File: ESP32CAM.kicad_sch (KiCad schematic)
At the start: 16 parts, among them J12 USB_C_Receptacle_USB2.0, SW6 SW_Push, U11 FT231XS, U12 ESP32-CAM

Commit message: Nearly done schematics
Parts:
- renumbered C24 to C25, C25 to C26, C26 to C27, C27 to C28, C28 to C29, SW6 to SW5
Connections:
- net 3.3V_Out: no longer R29.2, R30.1, U11.11 (USBDP), U11.12 (USBDM)
- new net: R30.1, U11.11 (USBDP)
- new net: R29.2, U11.12 (USBDM)

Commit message: Much much more progress
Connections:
- net 3.3V_Out: now also R29.2, R30.1, U11.11 (USBDP), U11.12 (USBDM)
- net ESPCAM_MISO: now also U12.P$12 (GPIO13); no longer U12.P$11 (GPIO12)
- net ESPCAM_MOSI: now also U12.P$11 (GPIO12); no longer U12.P$12 (GPIO13)
- net Earth: no longer SW5.2
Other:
- note added: "MISO"
- note added: "MOSI"
- moved on the sheet: C29, SW5, U12

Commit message: Rev 1
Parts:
- removed C29: 0.1uF, Capacitor_SMD:C_0402_1005Metric, symbol Device:C_Small
- removed R31: 1M, Resistor_SMD:R_0402_1005Metric, symbol Device:R_US
- removed SW5: SW_Push, Button_Switch_SMD:SW_SPST_PTS645, symbol Switch:SW_Push
- added J10: Conn_01x02, Connector_PinHeader_2.54mm:PinHeader_1x02_P2.54mm_Vertical, symbol Connector_Generic:Conn_01x02
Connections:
- net 3.3V_Out: no longer R29.2, R30.1, U11.11 (USBDP), U11.12 (USBDM)
- net Earth: now also J12.S1 (SHIELD), J10.1 (Pin_1)
- net at U12.P$6 (GPIO0): now also J10.2 (Pin_2)
- new net: R30.1, U11.11 (USBDP)
- new net: R29.2, U11.12 (USBDM)
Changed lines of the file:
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@@
   (junction (at 149.606 75.184) (diameter 0) (color 0 0 0 0)
-  )
-  (junction (at 129.286 44.704) (diameter 0) (color 0 0 0 0)
-  )
-  (junction (at 167.259 130.302) (diameter 0) (color 0 0 0 0)
-  )
-  (junction (at 129.286 47.244) (diameter 0) (color 0 0 0 0)
   )
   (junction (at 129.286 37.084) (diameter 0) (color 0 0 0 0)
@@
     (stroke (width 0) (type default))
   )
-  (wire (pts (xy 129.286 44.704) (xy 129.286 47.244))
-    (stroke (width 0) (type default))
-  )
-  (wire (pts (xy 25.4 66.04) (xy 25.4 65.405))
-    (stroke (width 0) (type default))
-  )
   (wire (pts (xy 131.826 20.574) (xy 138.176 20.574))
     (stroke (width 0) (type default))
@@
     (stroke (width 0) (type default))
   )
-  (wire (pts (xy 129.286 37.084) (xy 129.286 44.704))
+  (wire (pts (xy 129.286 37.084) (xy 129.286 52.324))
     (stroke (width 0) (type default))
   )
@@
     (stroke (width 0) (type default))
   )
-  (wire (pts (xy 169.799 134.112) (xy 167.259 134.112))
-    (stroke (width 0) (type default))
-  )
   (wire (pts (xy 57.15 45.085) (xy 48.26 45.085))
     (stroke (width 0) (type default))
@@
     (stroke (width 0) (type default))
   )
-  (wire (pts (xy 167.259 130.302) (xy 167.259 134.112))
-    (stroke (width 0) (type default))
-  )
   (wire (pts (xy 105.029 130.302) (xy 112.014 130.302))
     (stroke (width 0) (type default))
@@
     (stroke (width 0) (type default))
   )
-  (wire (pts (xy 174.879 134.112) (xy 177.419 134.112))
-    (stroke (width 0) (type default))
-  )
   (wire (pts (xy 113.411 44.704) (xy 115.316 44.704))
     (stroke (width 0) (type default))
@@
     (stroke (width 0) (type default))
   )
-  (wire (pts (xy 129.286 47.244) (xy 129.286 52.324))
-    (stroke (width 0) (type default))
-  )
   (wire (pts (xy 48.26 40.005) (xy 48.26 42.545))
     (stroke (width 0) (type default))
@@
     (stroke (width 0) (type default))
   )
+  (wire (pts (xy 167.259 136.017) (xy 167.259 132.842))
+    (stroke (width 0) (type default))
+  )
   (wire (pts (xy 121.666 37.084) (xy 121.666 36.449))
     (stroke (width 0) (type default))
@@
     (stroke (width 0) (type default))
   )
-  (wire (pts (xy 25.4 73.66) (xy 25.4 74.93))
+  (wire (pts (xy 25.4 65.405) (xy 25.4 74.93))
     (stroke (width 0) (type default))
   )
@@
     )
   )
-  (symbol (lib_id "Switch:SW_Push") (at 172.339 130.302 0) (unit 1)
-    (in_bom yes) (on_board yes) (dnp no) (fields_autoplaced)
-    (property "Reference" "SW5" (at 172.339 122.047 0)
-      (effects (font (size 1.27 1.27)))
-    )
-    (property "Value" "SW_Push" (at 172.339 124.587 0)
-      (effects (font (size 1.27 1.27)))
-    )
-    (property "Footprint" "Button_Switch_SMD:SW_SPST_PTS645" (at 172.339 125.222 0)
-      (effects (font (size 1.27 1.27)) hide)
-    )
-    (property "Datasheet" "~" (at 172.339 125.222 0)
-      (effects (font (size 1.27 1.27)) hide)
-    )
-    (pin "1")
-    (pin "2")
-    (instances
-      (project "DeltaRhoRobot"
-        (path "/cced1a6d-3dc4-42b2-93bd-998a7b4cf4e8/5eb80655-957d-4a1c-8d7d-b2e173715026/ba807c80-2a51-4f5f-8aa4-02e2ddffef6a"
-          (reference "SW5") (unit 1)
-        )
-      )
-    )
-  )
-  (symbol (lib_id "power:Earth") (at 177.419 134.112 0) (unit 1)
-    (in_bom yes) (on_board yes) (dnp no) (fields_autoplaced)
-    (property "Reference" "#PWR0104" (at 177.419 140.462 0)
-      (effects (font (size 1.27 1.27)) hide)
-    )
-    (property "Value" "Earth" (at 177.419 137.922 0)
-      (effects (font (size 1.27 1.27)) hide)
-    )
-    (property "Footprint" "" (at 177.419 134.112 0)
-      (effects (font (size 1.27 1.27)) hide)
-    )
-    (property "Datasheet" "~" (at 177.419 134.112 0)
+  (symbol (lib_id "power:Earth") (at 167.259 136.017 0) (unit 1)
+    (in_bom yes) (on_board yes) (dnp no) (fields_autoplaced)
+    (property "Reference" "#PWR0104" (at 167.259 142.367 0)
+      (effects (font (size 1.27 1.27)) hide)
+    )
+    (property "Value" "Earth" (at 167.259 139.827 0)
+      (effects (font (size 1.27 1.27)) hide)
+    )
+    (property "Footprint" "" (at 167.259 136.017 0)
+      (effects (font (size 1.27 1.27)) hide)
+    )
+    (property "Datasheet" "~" (at 167.259 136.017 0)
       (effects (font (size 1.27 1.27)) hide)
     )
@@
     )
   )
-  (symbol (lib_id "Device:C_Small") (at 172.339 134.112 270) (unit 1)
-    (in_bom yes) (on_board yes) (dnp no)
-    (property "Reference" "C29" (at 169.164 137.287 90)
-      (effects (font (size 1.27 1.27)) (justify left))
-    )
-    (property "Value" "0.1uF" (at 169.164 139.192 90)
-      (effects (font (size 1.27 1.27)) (justify left))
-    )
-    (property "Footprint" "Capacitor_SMD:C_0402_1005Metric" (at 172.339 134.112 0)
-      (effects (font (size 1.27 1.27)) hide)
-    )
-    (property "Datasheet" "~" (at 172.339 134.112 0)
-      (effects (font (size 1.27 1.27)) hide)
-    )
-    (pin "1")
-    (pin "2")
-    (instances
-      (project "DeltaRhoRobot"
-        (path "/cced1a6d-3dc4-42b2-93bd-998a7b4cf4e8/5eb80655-957d-4a1c-8d7d-b2e173715026/ba807c80-2a51-4f5f-8aa4-02e2ddffef6a"
-          (reference "C29") (unit 1)
-        )
-      )
-    )
-  )
   (symbol (lib_id "power:Earth") (at 164.719 123.317 0) (mirror y) (unit 1)
     (in_bom yes) (on_board yes) (dnp no) (fields_autoplaced)
@@
         (path "/cced1a6d-3dc4-42b2-93bd-998a7b4cf4e8/5eb80655-957d-4a1c-8d7d-b2e173715026/ba807c80-2a51-4f5f-8aa4-02e2ddffef6a"
           (reference "R29") (unit 1)
+        )
+      )
+    )
+  )
+  (symbol (lib_id "Connector_Generic:Conn_01x02") (at 172.339 132.842 0) (mirror x) (unit 1)
+    (in_bom yes) (on_board yes) (dnp no)
+    (property "Reference" "J10" (at 175.26 132.842 0)
+      (effects (font (size 1.27 1.27)) (justify left))
+    )
+    (property "Value" "Conn_01x02" (at 175.26 130.302 0)
+      (effects (font (size 1.27 1.27)) (justify left))
+    )
+    (property "Footprint" "Connector_PinHeader_2.54mm:PinHeader_1x02_P2.54mm_Vertical" (at 172.339 132.842 0)
+      (effects (font (size 1.27 1.27)) hide)
+    )
+    (property "Datasheet" "~" (at 172.339 132.842 0)
+      (effects (font (size 1.27 1.27)) hide)
+    )
+    (pin "1")
+    (pin "2")
+    (instances
+      (project "DeltaRhoRobot"
+        (path "/cced1a6d-3dc4-42b2-93bd-998a7b4cf4e8/5eb80655-957d-4a1c-8d7d-b2e173715026/ba807c80-2a51-4f5f-8aa4-02e2ddffef6a"
+          (reference "J10") (unit 1)
         )
       )
@@
         )
       )
-    )
-  )
-  (symbol (lib_id "Device:R_US") (at 25.4 69.85 0) (unit 1)
-    (in_bom yes) (on_board yes) (dnp no) (fields_autoplaced)
-    (property "Reference" "R31" (at 27.94 68.58 0)
-      (effects (font (size 1.27 1.27)) (justify left))
-    )
-    (property "Value" "1M" (at 27.94 71.12 0)
-      (effects (font (size 1.27 1.27)) (justify left))
-    )
-    (property "Footprint" "Resistor_SMD:R_0402_1005Metric" (at 26.416 70.104 90)
-      (effects (font (size 1.27 1.27)) hide)
-    )
-    (property "Datasheet" "~" (at 25.4 69.85 0)
-      (effects (font (size 1.27 1.27)) hide)
-    )
-    (pin "1")
-    (pin "2")
-    (instances
-      (project "DeltaRhoRobot"
-        (path "/cced1a6d-3dc4-42b2-93bd-998a7b4cf4e8/5eb80655-957d-4a1c-8d7d-b2e173715026/ba807c80-2a51-4f5f-8aa4-02e2ddffef6a"
-          (reference "R31") (unit 1)
-        )
-      )

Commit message: Rev0.1
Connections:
- net ESPCAM_MISO: now also U12.P$11 (GPIO12); no longer U12.P$12 (GPIO13)
- net ESPCAM_MOSI: now also U12.P$12 (GPIO13); no longer U12.P$11 (GPIO12)
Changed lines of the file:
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@@
     (effects (font (size 1.27 1.27)) (justify left))
   )
-  (hierarchical_label "ESPCAM_MISO" (shape input) (at 105.029 127.762 180) (fields_autoplaced)
+  (hierarchical_label "ESPCAM_MISO" (shape input) (at 105.029 130.302 180) (fields_autoplaced)
     (effects (font (size 1.27 1.27)) (justify right))
   )
@@
     (effects (font (size 1.27 1.27)) (justify left))
   )
-  (hierarchical_label "ESPCAM_MOSI" (shape output) (at 105.029 130.302 180) (fields_autoplaced)
+  (hierarchical_label "ESPCAM_MOSI" (shape output) (at 105.029 127.762 180) (fields_autoplaced)
     (effects (font (size 1.27 1.27)) (justify right))
   )

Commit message: clean up Rev
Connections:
- net 3.3V_Out: now also R29.2, R30.1, U11.11 (USBDP), U11.12 (USBDM)

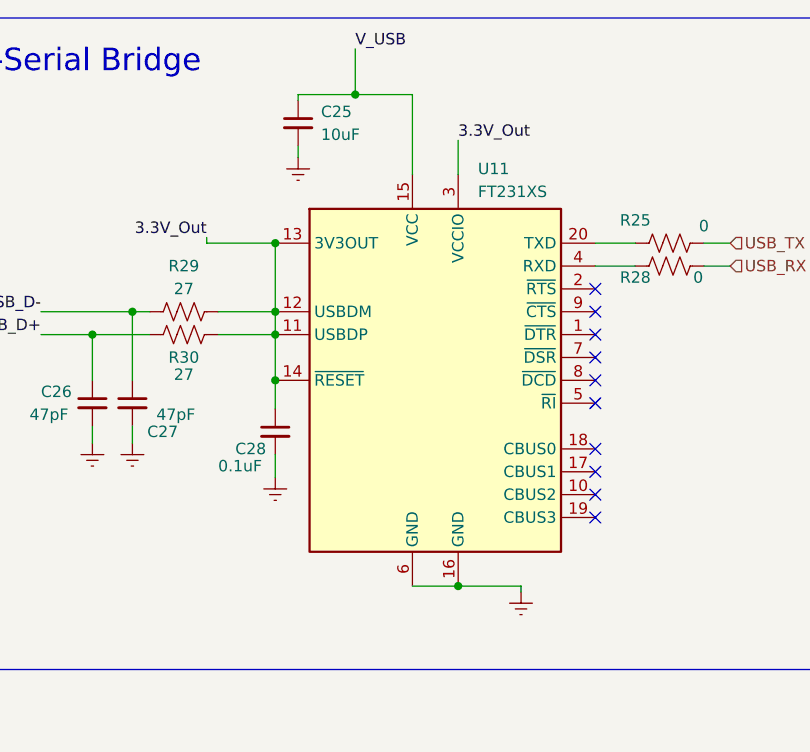
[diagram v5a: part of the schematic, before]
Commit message: Removed 201-sized parts
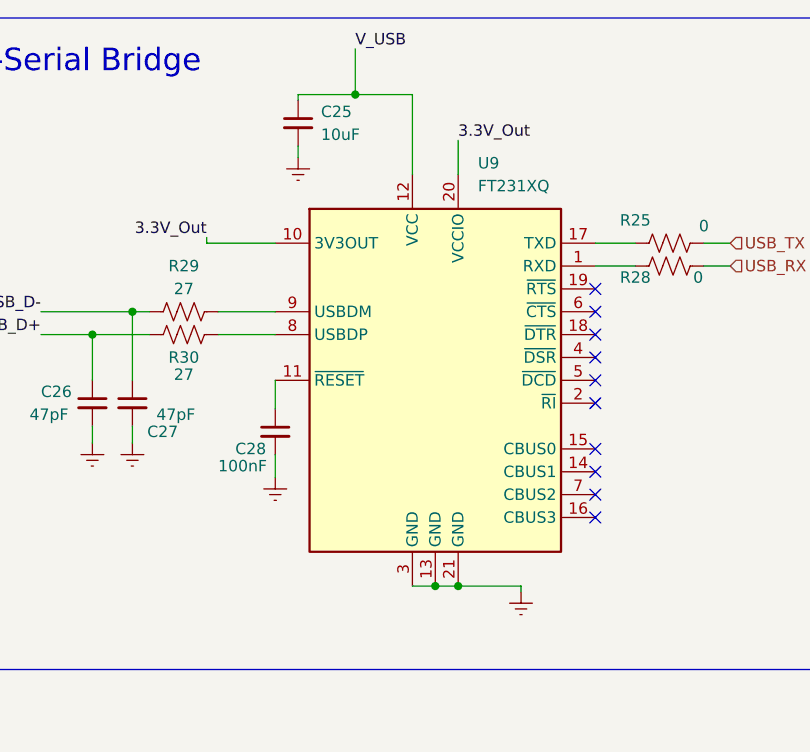
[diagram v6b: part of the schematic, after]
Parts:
- removed U11: FT231XS, Package_SO:SSOP-20_3.9x8.7mm_P0.635mm, symbol Interface_USB:FT231XS
- added U9: FT231XQ, Package_DFN_QFN:QFN-20-1EP_4x4mm_P0.5mm_EP2.5x2.5mm, symbol Interface_USB:FT231XQ
- C25: LCSC Part # (none) -> C15525
- C26, C27: LCSC Part # (none) -> C76970
- C28: value 0.1uF -> 100nF; LCSC Part # (none) -> C77020
- J12: footprint Connector_USB:USB_C_Receptacle_GCT_USB4105-xx-A_16P_TopMnt_Horizontal -> Connector_USB:USB_C_Receptacle_G-Switch_GT-USB-7010ASV; LCSC Part # (none) -> C2988369
- R26, R27: LCSC Part # (none) -> C477765
- R29, R30: LCSC Part # (none) -> C278580
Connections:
- net 3.3V_Out: now also U9.10 (3V3OUT), U9.20 (VCCIO); no longer C28.1, R29.2, R30.1
- net Earth: now also U9.13 (GND), U9.21 (GND), U9.3 (GND)
- net V_USB: now also U9.12 (VCC)
- net at R25.1: now also U9.17 (TXD)
- net at R28.2: now also U9.1 (RXD)
- new net: C28.1, U9.11 (~{RESET})
- new net: R30.1, U9.8 (USBDP)
- new net: R29.2, U9.9 (USBDM)
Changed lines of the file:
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@@
   (junction (at 149.86 75.438) (diameter 0) (color 0 0 0 0)
   )
-  (junction (at 129.54 37.338) (diameter 0) (color 0 0 0 0)
-  )
-  (junction (at 129.54 44.958) (diameter 0) (color 0 0 0 0)
-  )
-  (junction (at 129.54 52.578) (diameter 0) (color 0 0 0 0)
-  )
   (junction (at 48.514 40.259) (diameter 0) (color 0 0 0 0)
   )
@@
   (junction (at 33.274 75.184) (diameter 0) (color 0 0 0 0)
   )
-  (junction (at 129.54 47.498) (diameter 0) (color 0 0 0 0)
+  (junction (at 147.32 75.438) (diameter 0) (color 0 0 0 0)
   )
   (junction (at 138.43 20.828) (diameter 0) (color 0 0 0 0)
@@
     (stroke (width 0) (type default))
   )
+  (wire (pts (xy 129.54 52.578) (xy 129.54 55.753))
+    (stroke (width 0) (type default))
+  )
   (wire (pts (xy 123.19 47.498) (xy 129.54 47.498))
     (stroke (width 0) (type default))
@@
     (stroke (width 0) (type default))
   )
-  (wire (pts (xy 129.54 37.338) (xy 129.54 44.958))
-    (stroke (width 0) (type default))
-  )
-  (wire (pts (xy 129.54 55.753) (xy 129.54 52.578))
-    (stroke (width 0) (type default))
-  )
   (wire (pts (xy 103.505 44.958) (xy 113.665 44.958))
     (stroke (width 0) (type default))
@@
     (stroke (width 0) (type default))
   )
-  (wire (pts (xy 129.54 44.958) (xy 129.54 47.498))
-    (stroke (width 0) (type default))
-  )
   (wire (pts (xy 165.1 39.878) (xy 169.545 39.878))
     (stroke (width 0) (type default))
@@
     (stroke (width 0) (type default))
   )
-  (wire (pts (xy 156.845 75.438) (xy 149.86 75.438))
+  (wire (pts (xy 144.78 75.438) (xy 147.32 75.438))
     (stroke (width 0) (type default))
   )
@@
     (stroke (width 0) (type default))
   )
+  (wire (pts (xy 149.86 75.438) (xy 156.845 75.438))
+    (stroke (width 0) (type default))
+  )
   (wire (pts (xy 138.43 15.748) (xy 138.43 20.828))
     (stroke (width 0) (type default))
   )
+  (wire (pts (xy 147.32 75.438) (xy 149.86 75.438))
+    (stroke (width 0) (type default))
+  )
   (wire (pts (xy 129.54 37.338) (xy 121.92 37.338))
     (stroke (width 0) (type default))
@@
     (stroke (width 0) (type default))
   )
-  (wire (pts (xy 144.78 75.438) (xy 149.86 75.438))
-    (stroke (width 0) (type default))
-  )
   (wire (pts (xy 161.163 128.016) (xy 147.828 128.016))
     (stroke (width 0) (type default))
@@
   )
   (wire (pts (xy 105.918 133.096) (xy 112.268 133.096))
-    (stroke (width 0) (type default))
-  )
-  (wire (pts (xy 129.54 47.498) (xy 129.54 52.578))
     (stroke (width 0) (type default))
   )
@@
       (effects (font (size 1.27 1.27)))
     )
-    (property "Footprint" "Connector_USB:USB_C_Receptacle_GCT_USB4105-xx-A_16P_TopMnt_Horizontal" (at 37.084 42.799 0)
+    (property "Footprint" "Connector_USB:USB_C_Receptacle_G-Switch_GT-USB-7010ASV" (at 37.084 42.799 0)
       (effects (font (size 1.27 1.27)) hide)
     )
     (property "Datasheet" "https://www.usb.org/sites/default/files/documents/usb_type-c.zip" (at 37.084 42.799 0)
+      (effects (font (size 1.27 1.27)) hide)
+    )
+    (property "LCSC Part #" "C2988369" (at 33.274 42.799 0)
       (effects (font (size 1.27 1.27)) hide)
     )
@@
     )
   )
+  (symbol (lib_id "Interface_USB:FT231XQ") (at 147.32 52.578 0) (unit 1)
+    (in_bom yes) (on_board yes) (dnp no) (fields_autoplaced)
+    (property "Reference" "U9" (at 152.0541 28.448 0)
+      (effects (font (size 1.27 1.27)) (justify left))
+    )
+    (property "Value" "FT231XQ" (at 152.0541 30.988 0)
+      (effects (font (size 1.27 1.27)) (justify left))
+    )
+    (property "Footprint" "Package_DFN_QFN:QFN-20-1EP_4x4mm_P0.5mm_EP2.5x2.5mm" (at 181.61 72.898 0)
+      (effects (font (size 1.27 1.27)) hide)
+    )
+    (property "Datasheet" "https://www.ftdichip.com/Support/Documents/DataSheets/ICs/DS_FT231X.pdf" (at 147.32 52.578 0)
+      (effects (font (size 1.27 1.27)) hide)
+    )
+    (property "LCSC Part #" "C132159" (at 147.32 52.578 0)
+      (effects (font (size 1.27 1.27)) hide)
+    )
+    (pin "17")
+    (pin "4")
+    (pin "6")
+    (pin "5")
+    (pin "10")
+    (pin "20")
+    (pin "14")
+    (pin "15")
+    (pin "13")
+    (pin "3")
+    (pin "2")
+    (pin "11")
+    (pin "12")
+    (pin "16")
+    (pin "9")
+    (pin "8")
+    (pin "19")
+    (pin "18")
+    (pin "7")
+    (pin "21")
+    (pin "1")
+    (instances
+      (project "DeltaRhoRobot"
+        (path "/cced1a6d-3dc4-42b2-93bd-998a7b4cf4e8/5eb80655-957d-4a1c-8d7d-b2e173715026/ba807c80-2a51-4f5f-8aa4-02e2ddffef6a"
+          (reference "U9") (unit 1)
+        )
+      )
+    )
+  )
   (symbol (lib_id "Device:C_Small") (at 129.54 58.293 0) (unit 1)
     (in_bom yes) (on_board yes) (dnp no)
@@
       (effects (font (size 1.27 1.27)) (justify left))
     )
-    (property "Value" "0.1uF" (at 123.19 62.103 0)
+    (property "Value" "100nF" (at 123.19 62.103 0)
       (effects (font (size 1.27 1.27)) (justify left))
     )
@@
     )
     (property "Datasheet" "~" (at 129.54 58.293 0)
+      (effects (font (size 1.27 1.27)) hide)
+    )
+    (property "LCSC Part #" "C77020" (at 129.54 58.293 0)
       (effects (font (size 1.27 1.27)) hide)
     )
@@
       (effects (font (size 1.27 1.27)) hide)
     )
+    (property "LCSC Part #" "C76970" (at 113.665 55.118 0)
+      (effects (font (size 1.27 1.27)) hide)
+    )
     (pin "2")
     (pin "1")
@@
     )
   )
-  (symbol (lib_id "Interface_USB:FT231XS") (at 147.32 52.578 0) (unit 1)
-    (in_bom yes) (on_board yes) (dnp no) (fields_autoplaced)
-    (property "Reference" "U11" (at 152.0541 29.083 0)
-      (effects (font (size 1.27 1.27)) (justify left))
-    )
-    (property "Value" "FT231XS" (at 152.0541 31.623 0)
-      (effects (font (size 1.27 1.27)) (justify left))
-    )
-    (property "Footprint" "Package_SO:SSOP-20_3.9x8.7mm_P0.635mm" (at 172.72 72.898 0)
-      (effects (font (size 1.27 1.27)) hide)
-    )
-    (property "Datasheet" "https://www.ftdichip.com/Support/Documents/DataSheets/ICs/DS_FT231X.pdf" (at 147.32 52.578 0)
-      (effects (font (size 1.27 1.27)) hide)
-    )
-    (pin "18")
-    (pin "11")
-    (pin "19")
-    (pin "13")
-    (pin "15")
-    (pin "5")
-    (pin "20")
-    (pin "2")
-    (pin "7")
-    (pin "16")
-    (pin "4")
-    (pin "1")
-    (pin "14")
-    (pin "17")
-    (pin "3")
-    (pin "8")
-    (pin "12")
-    (pin "9")
-    (pin "10")
-    (pin "6")
-    (instances
-      (project "DeltaRhoRobot"
-        (path "/cced1a6d-3dc4-42b2-93bd-998a7b4cf4e8/5eb80655-957d-4a1c-8d7d-b2e173715026/ba807c80-2a51-4f5f-8aa4-02e2ddffef6a"
-          (reference "U11") (unit 1)
-        )
-      )
-    )
-  )
   (symbol (lib_id "Device:C_Small") (at 132.08 24.003 0) (unit 1)
     (in_bom yes) (on_board yes) (dnp no) (fields_autoplaced)
@@
     )
     (property "Datasheet" "~" (at 132.08 24.003 0)
+      (effects (font (size 1.27 1.27)) hide)
+    )
+    (property "LCSC Part #" "C15525" (at 132.08 24.003 0)
       (effects (font (size 1.27 1.27)) hide)
     )
@@
     )
     (property "Datasheet" "~" (at 119.38 44.958 0)
+      (effects (font (size 1.27 1.27)) hide)
+    )
+    (property "LCSC Part #" "C278580" (at 119.38 44.958 0)
       (effects (font (size 1.27 1.27)) hide)
     )
@@
       (effects (font (size 1.27 1.27)) hide)
     )
+    (property "LCSC Part #" "C477765" (at 72.644 39.624 0)
+      (effects (font (size 1.27 1.27)) hide)
+    )
     (pin "1")
     (pin "2")
@@
       (effects (font (size 1.27 1.27)) hide)
     )
+    (property "LCSC Part #" "C76970" (at 109.22 55.118 0)
+      (effects (font (size 1.27 1.27)) hide)
+    )
     (pin "2")
     (pin "1")
@@
       (effects (font (size 1.27 1.27)) hide)
     )
+    (property "LCSC Part #" "C278580" (at 119.38 47.498 0)
+      (effects (font (size 1.27 1.27)) hide)
+    )
     (pin "2")
     (pin "1")
@@
       (effects (font (size 1.27 1.27)) hide)
     )
+    (property "LCSC Part #" "C477765" (at 65.024 39.624 0)
+      (effects (font (size 1.27 1.27)) hide)
+    )

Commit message: For production
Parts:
- C26, C27: LCSC Part # C76970 -> C1567
- C28: LCSC Part # C77020 -> C1525
- J12: JLCPCB Position Offset (none) -> 0.91,0
- R25, R28: LCSC Part # (none) -> C21376
- R26, R27: LCSC Part # C477765 -> C25905
- R29, R30: value 27 -> 33; LCSC Part # C278580 -> C25105

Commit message: JLCniceness
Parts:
- J12: JLCPCB Position Offset 0.91,0 -> 0,-0.91
- U9: JLCPCB Rotation Offset (none) -> 90
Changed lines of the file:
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@@
 			)
 		)
-		(property "JLCPCB Position Offset" "0.91,0"
+		(property "JLCPCB Position Offset" "0,-0.91"
 			(at 33.274 42.799 0)
 			(effects
@@
 			)
 		)
-		(property "JLCPCB Rotation Offset" ""
-			(at 147.32 52.578 0)
-			(effects
+		(property "JLCPCB Rotation Offset" "90"
+			(at 147.32 52.578 0)
+			(effects
